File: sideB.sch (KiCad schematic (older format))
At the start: 0 parts

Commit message: Started counter circuit
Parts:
- added D? (x4): LED, symbol LED
- added R? (x4): R, symbol R
- added U?: 4520, symbol 4520
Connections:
- new net: D?.1 (A), U?.3 (Q1)
- new net: D?.1 (A), U?.4 (Q2)
- new net: D?.1 (A), U?.5 (Q3)
- new net: D?.1 (A), U?.6 (Q4)
- new net: D?.2 (K), R?.1 (x4)
- new net GND: R?.2, R?.2, R?.2, R?.2
- new net VDD: U?.16 (VDD)
- new net VSS: U?.8 (VSS)
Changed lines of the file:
@@
-EESchema Schematic File Version 2  date Tue 11 Sep 2012 20:17:23 CEST
+EESchema Schematic File Version 2  date Wed 12 Sep 2012 05:38:18 PM CEST
 LIBS:power
 LIBS:device
@@
 LIBS:contrib
 LIBS:valves
-EELAYER 43  0
+EELAYER 25  0
 EELAYER END
 $Descr A4 11700 8267
@@
 Sheet 1 1
 Title ""
-Date "11 sep 2012"
+Date "12 sep 2012"
 Rev ""
 Comp ""
@@
 Comment4 ""
 $EndDescr
+Wire Wire Line
+	6000 3300 6000 3500
+Wire Wire Line
+	6550 3500 6550 3100
+Wire Wire Line
+	5250 2800 6250 2800
+Wire Wire Line
+	6000 4000 6000 4100
+Wire Wire Line
+	5700 4000 5700 4100
+Wire Wire Line
+	5250 3000 5700 3000
+Wire Wire Line
+	5700 3400 5700 3500
+Wire Wire Line
+	5250 2900 6000 2900
+Wire Wire Line
+	6250 4000 6250 4100
+Wire Wire Line
+	6550 4000 6550 4100
+Wire Wire Line
+	5250 2700 6550 2700
+Wire Wire Line
+	6250 3500 6250 3200
+$Comp
+L LED D?
+U 1 1 5050AC4D
+P 6250 3000
+F 0 "D?" H 6250 3100 50  0000 C CNN
+F 1 "LED" H 6250 2900 50  0000 C CNN
+	1    6250 3000
+	0    1    1    0
+$EndComp
+$Comp
+L R R?
+U 1 1 5050AC4C
+P 6250 3750
+F 0 "R?" V 6330 3750 50  0000 C CNN
+F 1 "R" V 6250 3750 50  0000 C CNN
+	1    6250 3750
+	1    0    0    -1
+$EndComp
+$Comp
+L GND #PWR?
+U 1 1 5050AC4B
+P 6250 4100
+F 0 "#PWR?" H 6250 4100 30  0001 C CNN
+F 1 "GND" H 6250 4030 30  0001 C CNN
+	1    6250 4100
+	1    0    0    -1
+$EndComp
+$Comp
+L GND #PWR?
+U 1 1 5050AC4A
+P 6550 4100
+F 0 "#PWR?" H 6550 4100 30  0001 C CNN
+F 1 "GND" H 6550 4030 30  0001 C CNN
+	1    6550 4100
+	1    0    0    -1
+$EndComp
+$Comp
+L R R?
+U 1 1 5050AC49
+P 6550 3750
+F 0 "R?" V 6630 3750 50  0000 C CNN
+F 1 "R" V 6550 3750 50  0000 C CNN
+	1    6550 3750
+	1    0    0    -1
+$EndComp
+$Comp
+L LED D?
+U 1 1 5050AC48
+P 6550 2900
+F 0 "D?" H 6550 3000 50  0000 C CNN
+F 1 "LED" H 6550 2800 50  0000 C CNN
+	1    6550 2900
+	0    1    1    0
+$EndComp
+$Comp
+L LED D?
+U 1 1 5050AC1D
+P 6000 3100
+F 0 "D?" H 6000 3200 50  0000 C CNN
+F 1 "LED" H 6000 3000 50  0000 C CNN
+	1    6000 3100
+	0    1    1    0
+$EndComp
+$Comp
+L R R?
+U 1 1 5050AC1C
+P 6000 3750
+F 0 "R?" V 6080 3750 50  0000 C CNN
+F 1 "R" V 6000 3750 50  0000 C CNN
+	1    6000 3750
+	1    0    0    -1
+$EndComp
+$Comp
+L GND #PWR?
+U 1 1 5050AC1B
+P 6000 4100
+F 0 "#PWR?" H 6000 4100 30  0001 C CNN
+F 1 "GND" H 6000 4030 30  0001 C CNN
+	1    6000 4100
+	1    0    0    -1
+$EndComp
+$Comp
+L GND #PWR?
+U 1 1 5050ABC3
+P 5700 4100
+F 0 "#PWR?" H 5700 4100 30  0001 C CNN
+F 1 "GND" H 5700 4030 30  0001 C CNN
+	1    5700 4100
+	1    0    0    -1
+$EndComp
+$Comp
+L R R?
+U 1 1 5050ABAA
+P 5700 3750
+F 0 "R?" V 5780 3750 50  0000 C CNN
+F 1 "R" V 5700 3750 50  0000 C CNN
+	1    5700 3750
+	1    0    0    -1
+$EndComp
+$Comp
+L LED D?
+U 1 1 5050AB99
+P 5700 3200
+F 0 "D?" H 5700 3300 50  0000 C CNN
+F 1 "LED" H 5700 3100 50  0000 C CNN
+	1    5700 3200
+	0    1    1    0
+$EndComp
+$Comp
+L 4520 U?
+U 1 1 5050AB85
+P 4650 3050
+F 0 "U?" H 4700 3500 60  0000 C CNN
+F 1 "4520" H 4850 2700 60  0000 C CNN
+	1    4650 3050
+	1    0    0    -1
+$EndComp
 $EndSCHEMATC

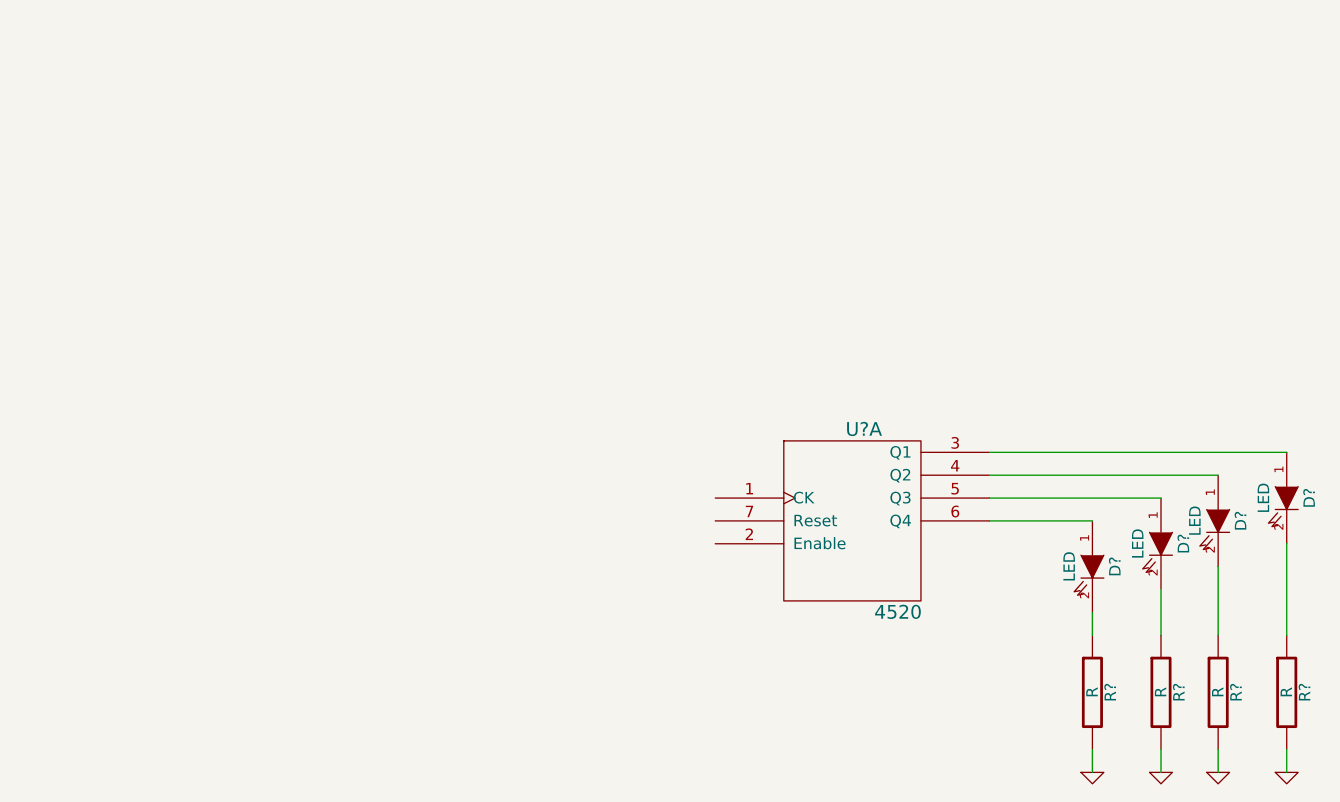
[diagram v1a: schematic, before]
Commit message: Binary counter circuit finished
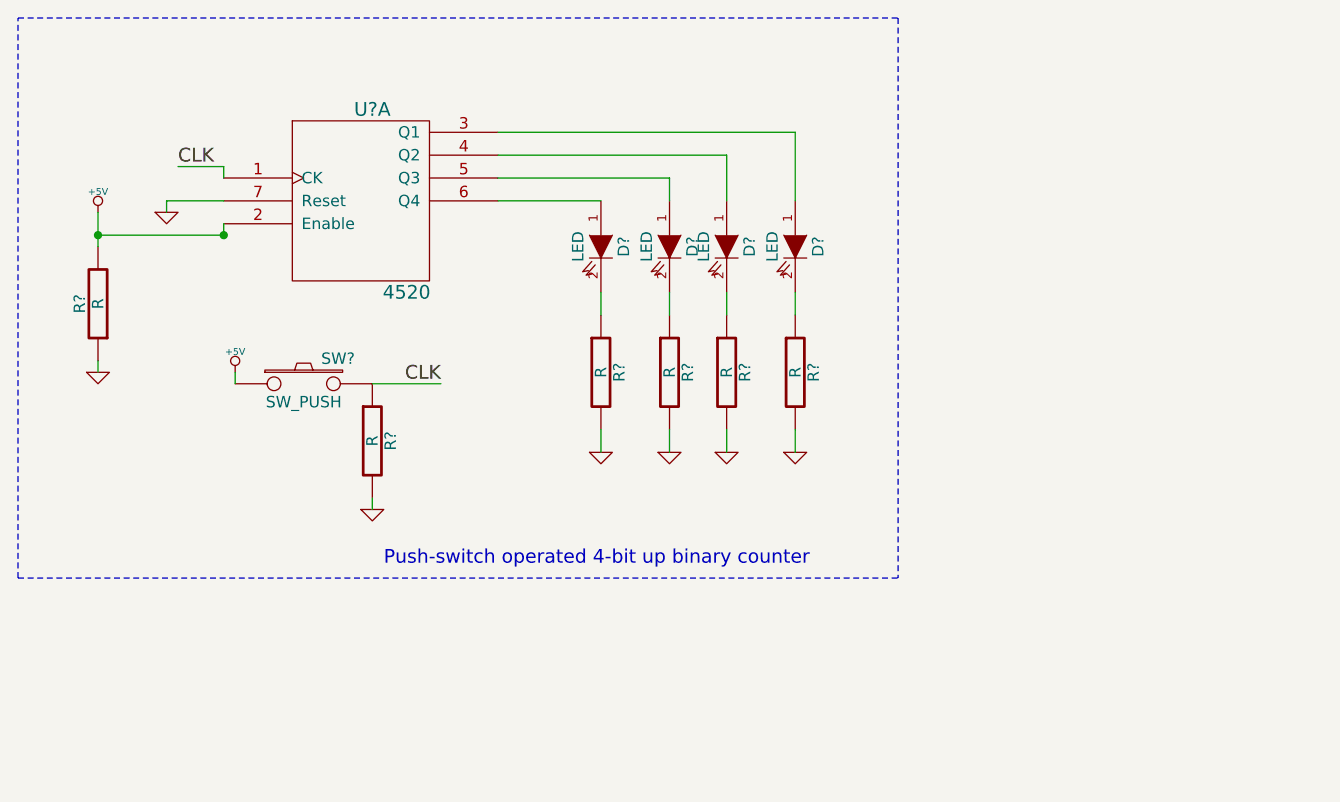
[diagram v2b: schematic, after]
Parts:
- added R? (x2): R, symbol R
- added SW?: SW_PUSH, symbol SW_PUSH
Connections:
- net GND: now also U?.7 (Reset), R?.1, R?.2
- net CLK: now reaches U?.1 (CK)
- net CLK: now also R?.1, SW?.2
- net +5V: now reaches U?.2 (Enable)
- net +5V: now also R?.2, SW?.1
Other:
- note added: "Push-switch operated 4-bit up binary counter"
- moved on the sheet: D?, R?, U?A

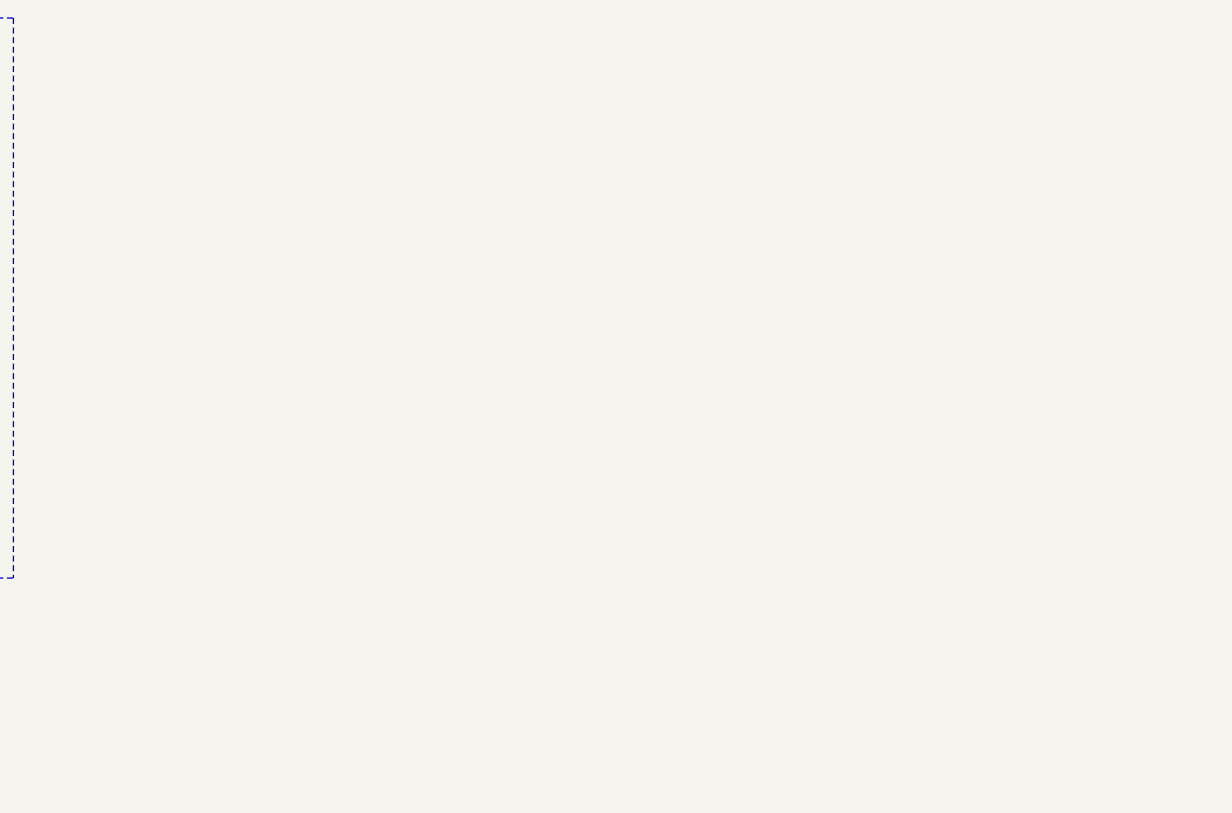
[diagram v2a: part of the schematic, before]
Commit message: ADC circuit added to schematic
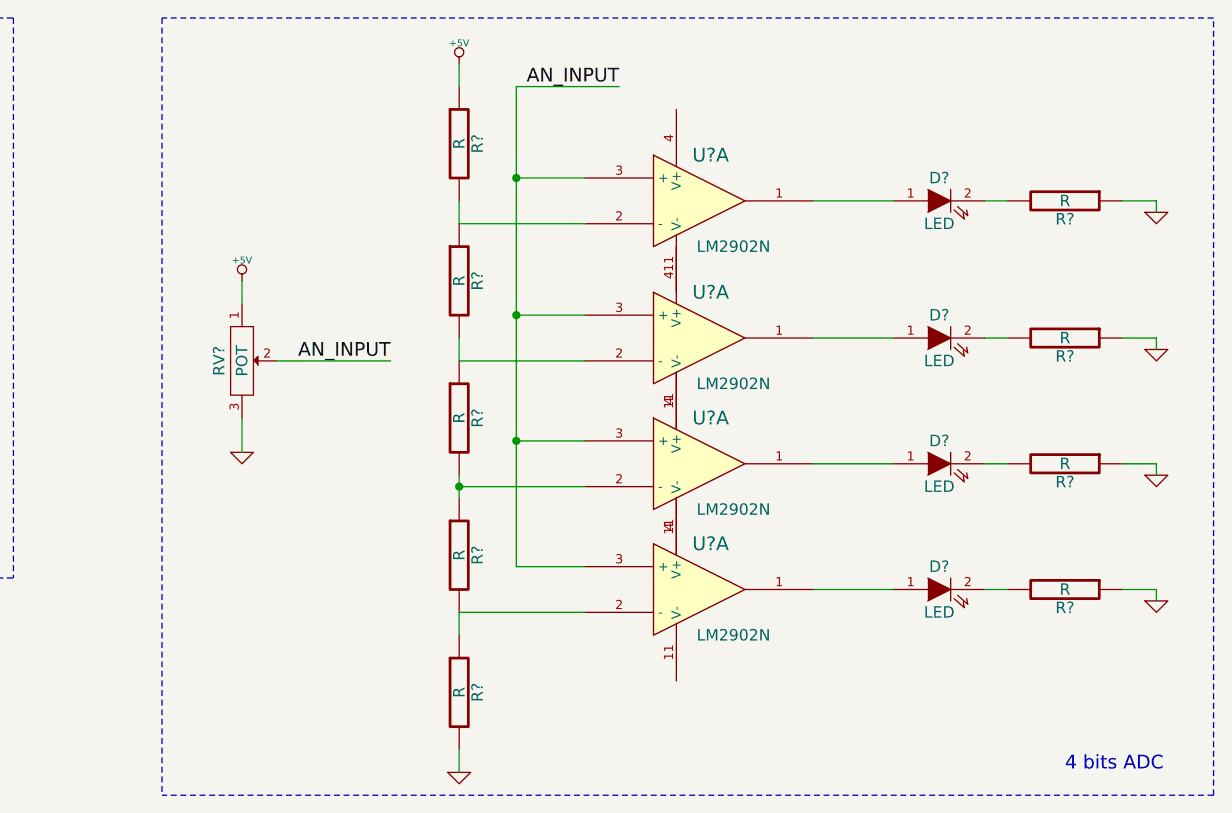
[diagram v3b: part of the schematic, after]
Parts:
- added D? (x4): LED, symbol LED
- added R? (x9): R, symbol R
- added RV?: POT, symbol POT
- added U? (x4): LM2902N, symbol LM2902N
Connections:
- net +5V: now also R?.1, RV?.1
- net GND: now also R?.1, R?.1, R?.1, R?.1, R?.2, RV?.3
- new net: D?.1 (A), U?.1 (x4)
- new net: R?.1, R?.2, U?.2 (-) (x4)
- new net: D?.2 (K), R?.2 (x4)
- new net AN_INPUT: RV?.2, U?.3 (+), U?.3 (+), U?.3 (+), U?.3 (+)
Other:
- note added: "4 bits ADC"

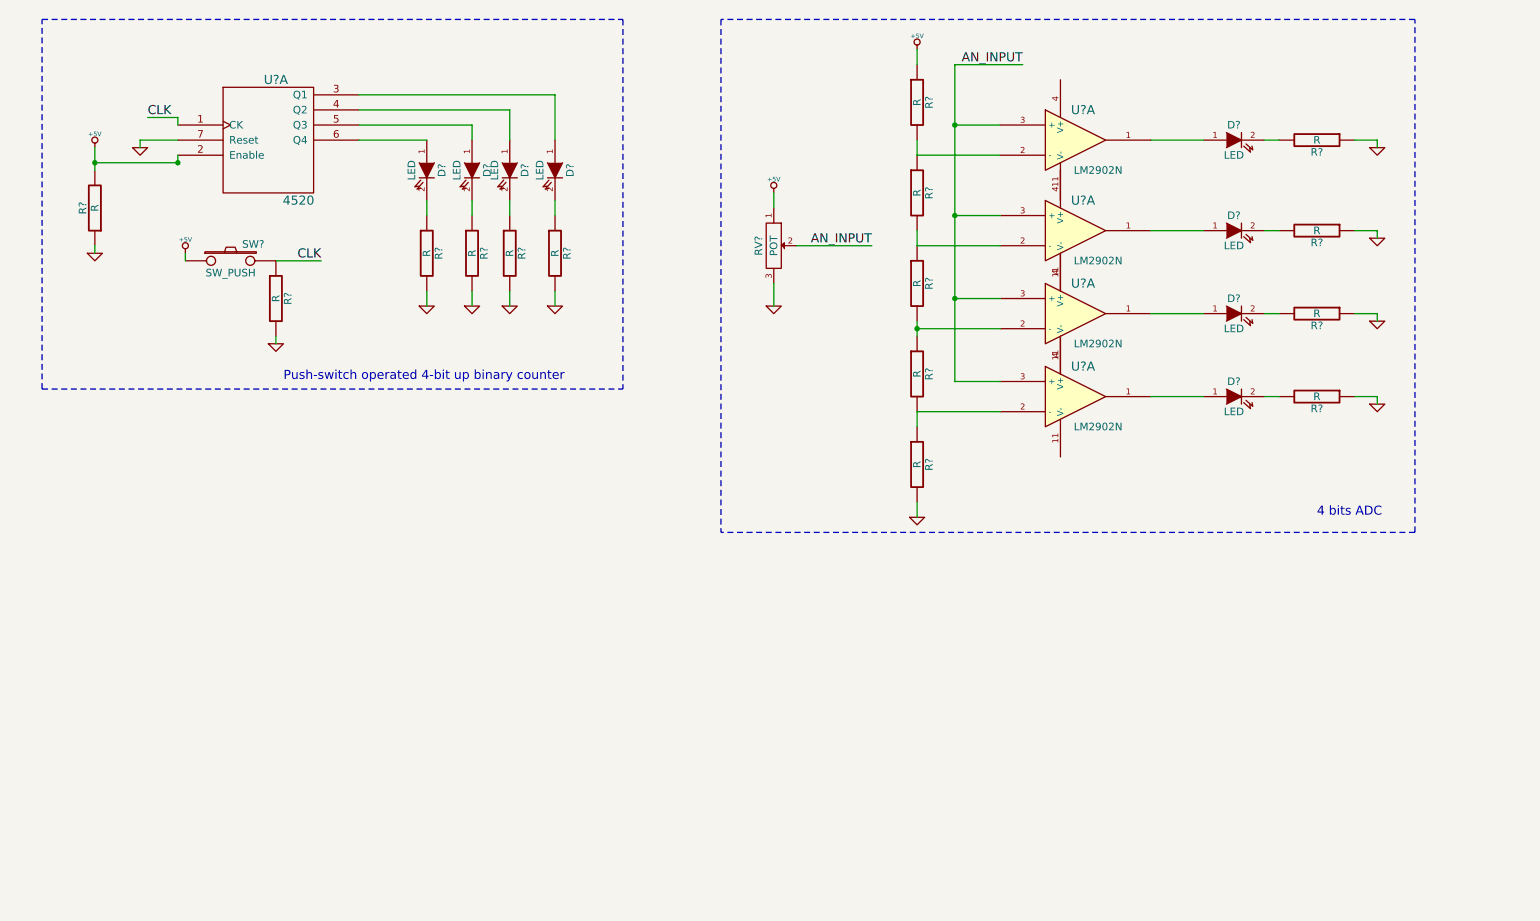
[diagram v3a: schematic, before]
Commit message: 555 added, not finished. Power supply added.
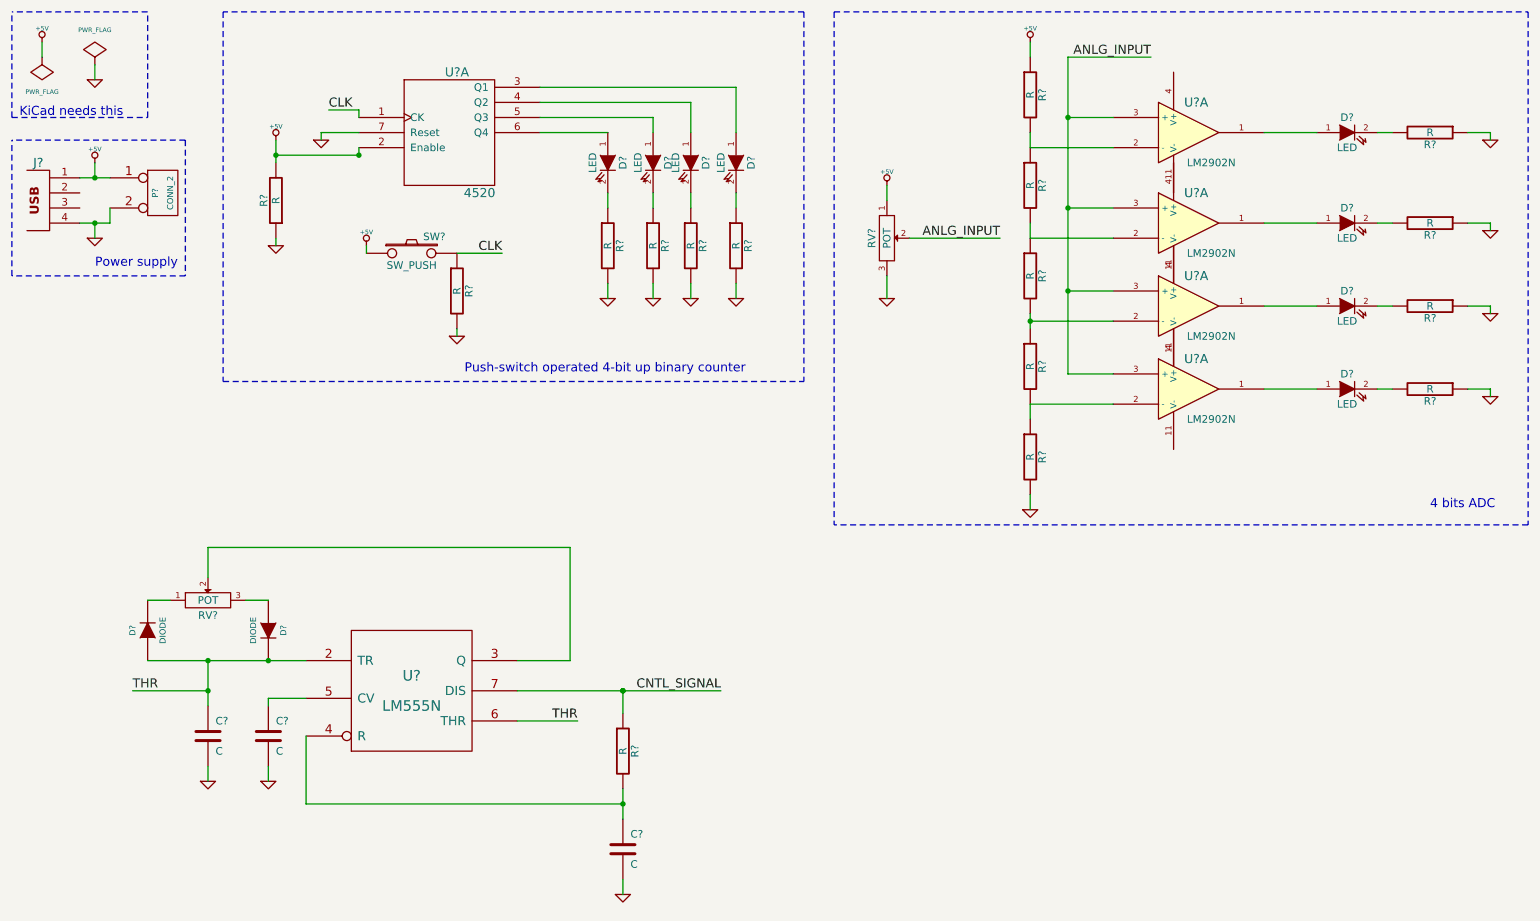
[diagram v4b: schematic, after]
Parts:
- added C? (x3): C, symbol C
- added D? (x2): DIODE, symbol DIODE
- added J?: USB_2, symbol USB_2
- added P?: CONN_2, symbol CONN_2
- added R?: R, symbol R
- added RV?: POT, symbol POT
- added U?: LM555N, symbol LM555N
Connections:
- net +5V: now also J?.1, P?.1 (P1)
- net GND: now also C?.2, C?.2, C?.2, J?.4, P?.2 (PM), U?.1 (GND)
- net AN_INPUT renamed ANLG_INPUT
- new net: RV?.2, U?.3 (Q)
- new net: C?.1, R?.2, U?.4 (R)
- new net: C?.1, U?.5 (CV)
- new net: D?.2 (K), RV?.1
- new net: D?.1 (A), RV?.3
- new net CNTL_SIGNAL: R?.1, U?.7 (DIS)
- new net THR: C?.1, D?.1 (A), D?.2 (K), U?.2 (TR), U?.6 (THR)
- new net VCC: U?.8 (VCC)
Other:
- note added: "KiCad needs this"
- note added: "Power supply"
- moved on the sheet: D?, R?, RV?, SW?, U?A

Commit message: Two choices added to 555 circuit.
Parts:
- added D? (x2): LED, symbol LED
- added Q?: NPN, symbol NPN
- added Q?: MOSFET_N, symbol MOSFET_N
- added R? (x2): R, symbol R
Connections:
- wire segments 88 -> 98
- no-connect marks 0 -> 2
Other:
- note added: "MOSFET option"
- note added: "NPN option\n"
- moved on the sheet: C?, D?, R?, RV?, U?

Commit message: 555 design finished.
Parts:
- removed D?: LED, symbol LED
- removed Q?: MOSFET_N, symbol MOSFET_N
- removed R?: R, symbol R
- added U?: LM2902N, symbol LM2902N
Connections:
- net labels removed: CNTL_SIGNAL
- wire segments 98 -> 92
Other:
- note added: "555-based PWM dimmer"
- note removed: "MOSFET option"
- note removed: "NPN option\n"
- moved on the sheet: C?, D?, Q?, R?, RV?, U?

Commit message: Schematic Annotated
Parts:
- gave numbers to parts that had none: 40
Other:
- moved on the sheet: IC2E

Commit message: Annotated and ERC checked
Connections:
- net VCC is gone; now on net +5V: IC3.8 (VCC)
- net VDD is gone; now on net +5V: IC1.16 (VDD)
- net VSS is gone; now on net GND: IC1.8 (VSS)
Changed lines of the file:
@@
-EESchema Schematic File Version 2  date Wed 19 Sep 2012 04:55:25 PM CEST
+EESchema Schematic File Version 2  date Wed 19 Sep 2012 18:42:47 CEST
 LIBS:power
 LIBS:device
@@
 $EndDescr
 Wire Wire Line
+	3500 5500 3500 5400
+Wire Wire Line
+	3550 1950 3550 1900
+Wire Wire Line
 	6850 2950 6850 2900
 Wire Notes Line
@@
 	1350 2250 1350 2150
 Wire Wire Line
-	1450 1850 1250 1850
+	1250 1850 1450 1850
 Wire Wire Line
 	2550 5100 2550 5050
@@
 Connection ~ 2550 4800
 Wire Wire Line
-	2800 4800 1750 4800
+	1750 4800 2800 4800
 Wire Notes Line
 	10850 4150 6250 4150
@@
 	2850 1550 2850 1600
 Wire Wire Line
-	2550 1750 2550 1600
+	2550 1600 2550 1750
 Wire Wire Line
 	3100 1650 3100 1700
@@
 	7550 1650 7550 1550
 Wire Wire Line
-	7550 2750 7550 2850
+	7550 2850 7550 2750
 Wire Wire Line
 	7550 3950 7550 4050
@@
 Connection ~ 4900 5000
 Wire Wire Line
-	4900 5650 4900 5850
+	4900 5850 4900 5650
 Connection ~ 4900 5750
 Wire Wire Line
@@
 	2150 5500 2150 5600
 Wire Wire Line
-	2150 4800 2150 5100
+	2150 5100 2150 4800
 Connection ~ 2150 5000
 Wire Wire Line
@@
 	5600 4750 5600 4800
 Wire Wire Line
-	5300 5000 4200 5000
+	4200 5000 5300 5000
 Wire Notes Line
 	6050 3500 6050 6650
 Wire Wire Line
 	6850 3900 6850 3850
+Wire Wire Line
+	3550 1200 3550 1100
+Wire Wire Line
+	3500 4500 3500 4600
+$Comp
+L GND #PWR?
+U 1 1 5059F5FF
+P 3500 5500
+F 0 "#PWR?" H 3500 5500 30  0001 C CNN
+F 1 "GND" H 3500 5430 30  0001 C CNN
+	1    3500 5500
+	1    0    0    -1
+$EndComp
+$Comp
+L +5V #PWR?
+U 1 1 5059F5F6
+P 3500 4500
+F 0 "#PWR?" H 3500 4590 20  0001 C CNN
+F 1 "+5V" H 3500 4590 30  0000 C CNN
+	1    3500 4500
+	1    0    0    -1
+$EndComp
+$Comp
+L GND #PWR?
+U 1 1 5059F5E5
+P 3550 1950
+F 0 "#PWR?" H 3550 1950 30  0001 C CNN
+F 1 "GND" H 3550 1880 30  0001 C CNN
+	1    3550 1950
+	1    0    0    -1
+$EndComp
+$Comp
+L +5V #PWR?
+U 1 1 5059F5D2
+P 3550 1100
+F 0 "#PWR?" H 3550 1190 20  0001 C CNN
+F 1 "+5V" H 3550 1190 30  0000 C CNN
+	1    3550 1100
+	1    0    0    -1
+$EndComp
 $Comp
 L +5V #PWR01
